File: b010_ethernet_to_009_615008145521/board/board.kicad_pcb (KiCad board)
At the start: 2 copper layers, 21 x 29 mm, 2 parts, among them J1 009_1000BASE-T_2x5, J2 RJ45_Shielded

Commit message: version 3
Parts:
- added R1: 0R, Resistor_SMD:R_0603_1608Metric, F.Cu at (128.5, 87.8)
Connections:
- J1 pad 3: Earth -> Net-(J1-Pad3)
- J1 pad 6: Net-(J1-Pad6) -> Earth
- J2 pad 1: Net-(J1-Pad10) -> Net-(J1-Pad3)
- J2 pad 2: Net-(J1-Pad6) -> Net-(J1-Pad2)
- J2 pad 3: Net-(J1-Pad4) -> Net-(J1-Pad5)
- J2 pad 4: Net-(J1-Pad8) -> Net-(J1-Pad7)
- J2 pad 5: Net-(J1-Pad9) -> Net-(J1-Pad8)
- J2 pad 6: Net-(J1-Pad5) -> Net-(J1-Pad4)
- J2 pad 7: Net-(J1-Pad2) -> Net-(J1-Pad9)
- J2 pad 8: Net-(J1-Pad7) -> Net-(J1-Pad10)
- J2 pad SH: Earth -> Net-(J2-PadSH)
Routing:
- net Earth: track 37.9 -> 6.31 mm, vias 1 -> 0
- net Net-(J2-PadSH): track 0.00 -> 29.0 mm
- net Net-(J1-Pad3): track 0.00 -> 21.4 mm
- net Net-(J1-Pad6): track 21.0 -> 0.00 mm
- net Net-(J1-Pad7): track 31.9 -> 17.0 mm
- net Net-(J1-Pad9): track 15.5 -> 30.4 mm
- net Net-(J1-Pad10): track 17.2 -> 28.4 mm
- net Net-(J1-Pad2): track 34.2 -> 27.0 mm
- net Net-(J1-Pad8): track 18.2 -> 14.7 mm, vias 1 -> 0
- net Net-(J1-Pad5): track 18.5 -> 17.7 mm
- net Net-(J1-Pad4): track 15.1 -> 15.3 mm, vias 1 -> 0
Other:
- board text added: "osf.b010.v0.3"
- board text removed: "osf.b010.v0.1"

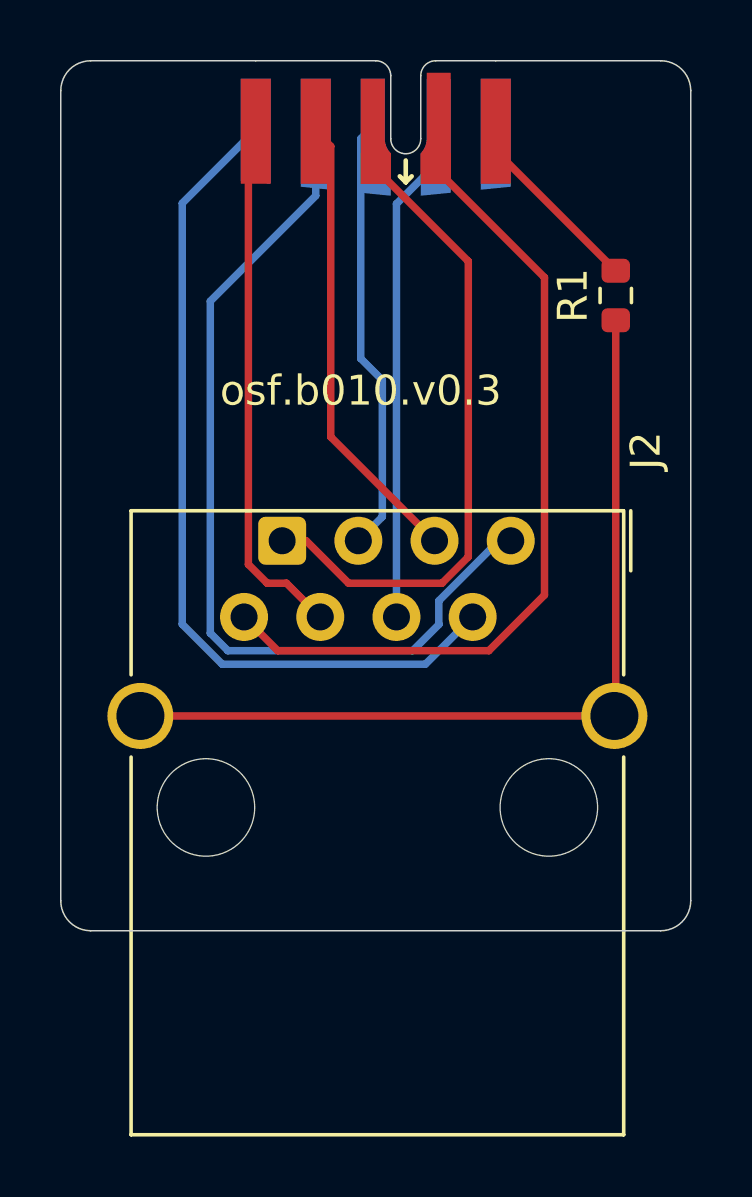
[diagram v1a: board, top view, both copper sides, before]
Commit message: updated to kicad 6
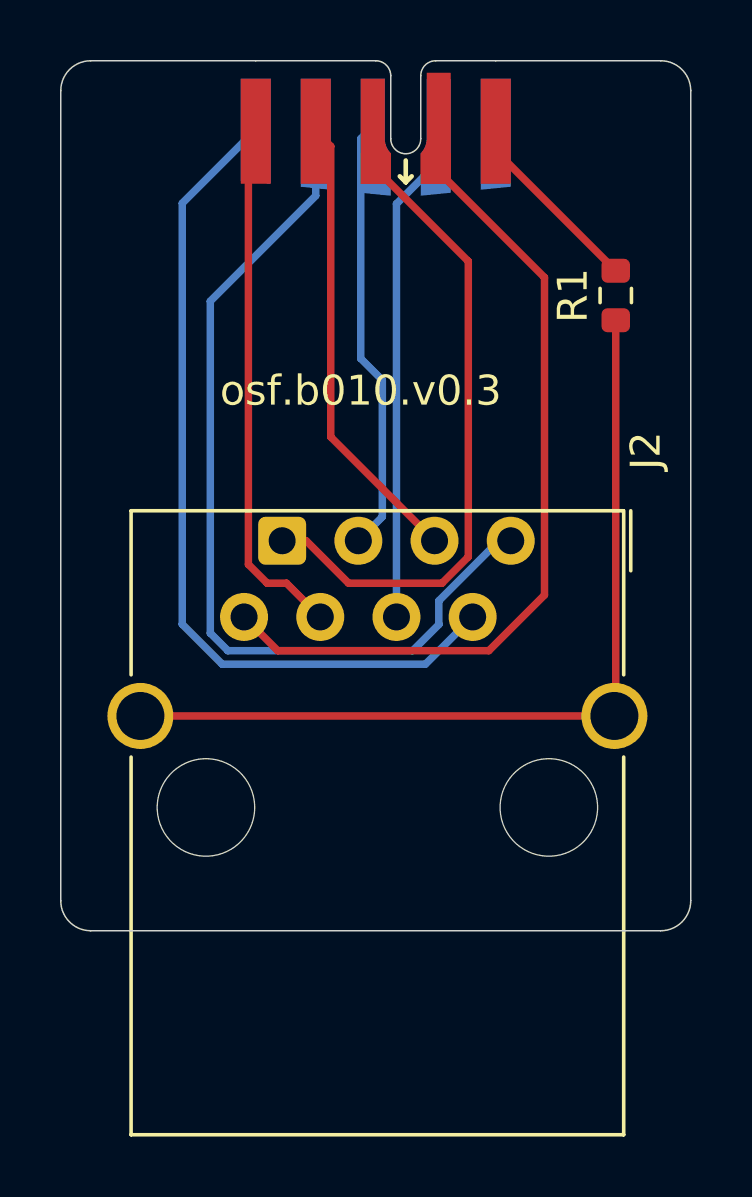
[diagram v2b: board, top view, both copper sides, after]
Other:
- net class Default removed
